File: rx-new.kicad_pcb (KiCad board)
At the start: 2 copper layers, 76.2 x 57.1 mm, 96 parts, among them J1 RF_IN, J2 PWR_IN, J3 IQ_OUT, J4 4LO_IN, Q1 BC848, Q2 BC858, Q3 BC848, Q4 BC858, U1 TPS79101DBVREP, U2 SN74CBT3253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

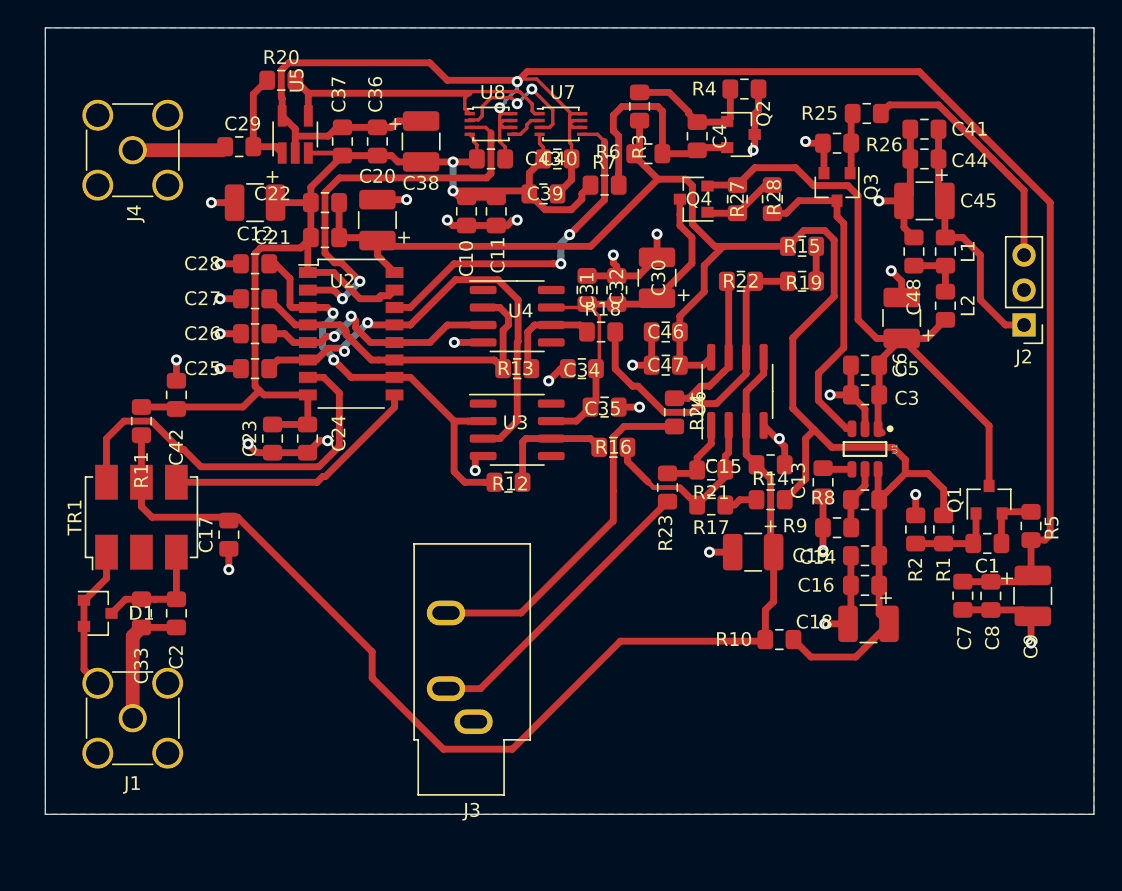
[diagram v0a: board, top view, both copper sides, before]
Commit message: Added mounting holes and small layout changes
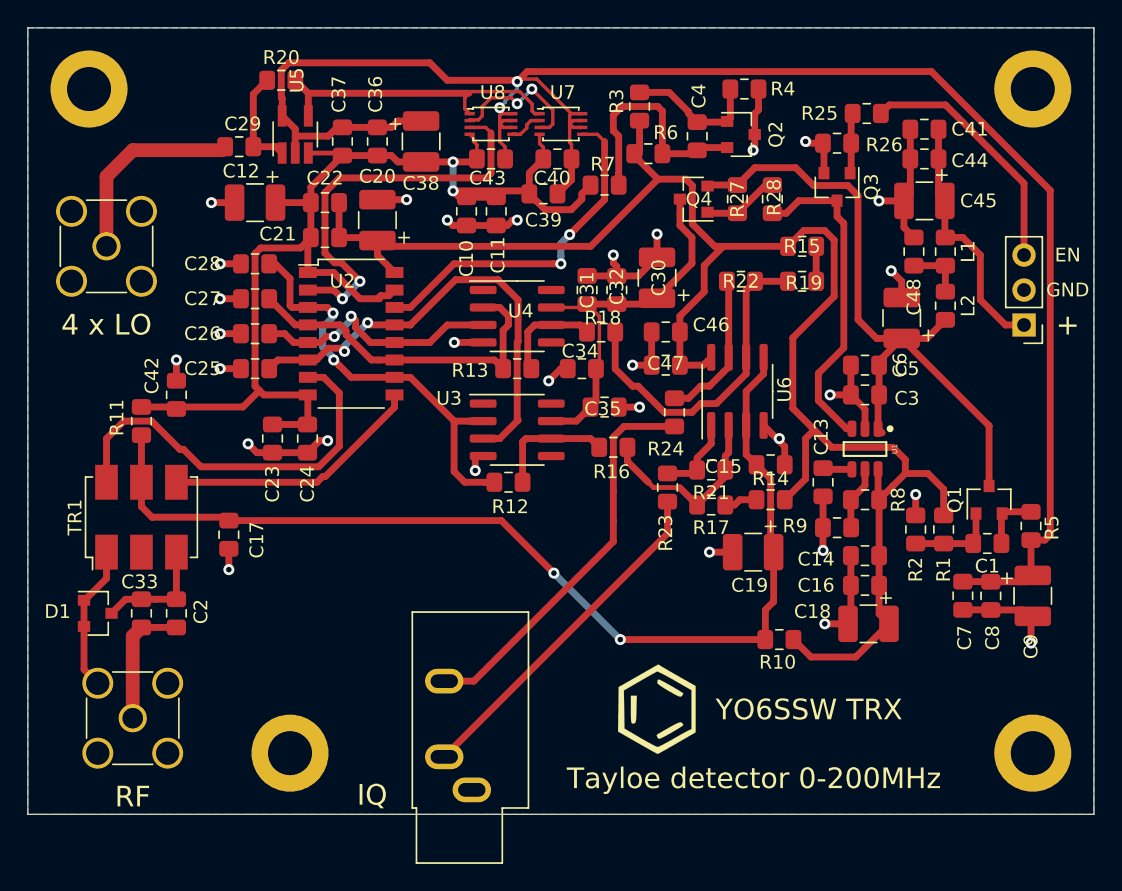
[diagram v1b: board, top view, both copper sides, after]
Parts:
- added G***: LOGO, benzen_logos:benzene_only_logo, F.Cu at (108.0, 94.0)
- added H1: MountingHole_Pad, MountingHole:MountingHole_3.2mm_M3_DIN965_Pad, F.Cu at (135.3, 48.9)
- added H2: MountingHole_Pad, MountingHole:MountingHole_3.2mm_M3_DIN965_Pad, F.Cu at (66.7, 48.9)
- added H3: MountingHole_Pad, MountingHole:MountingHole_3.2mm_M3_DIN965_Pad, F.Cu at (135.3, 97.2)
- added H4: MountingHole_Pad, MountingHole:MountingHole_3.2mm_M3_DIN965_Pad, F.Cu at (81.3, 97.2)
- moved J4 7.24 mm to (67.9, 60.3)
- moved J3 4.95 mm to (94.5, 99.8)
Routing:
- net Net-(C29-Pad2): track 6.82 -> 14.6 mm
- net /Vbias: track 85.0 -> 77.3 mm, vias 0 -> 2
- net /AUDIO_I: track 22.0 -> 25.5 mm
- net /AUDIO_Q: track 25.8 -> 28.9 mm
- net /+Vd: track 134.0 -> 134.5 mm
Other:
- board size 76.2 x 57.1 mm -> 77.5 x 57.1 mm
- board text added: "+"
- board text added: "4 x LO"
- board text added: "EN"
- board text added: "GND"
- board text added: "IQ"
- board text added: "RF"
- board text added: "Tayloe detector 0-200MHz"
- board text added: "YO6SSW TRX"

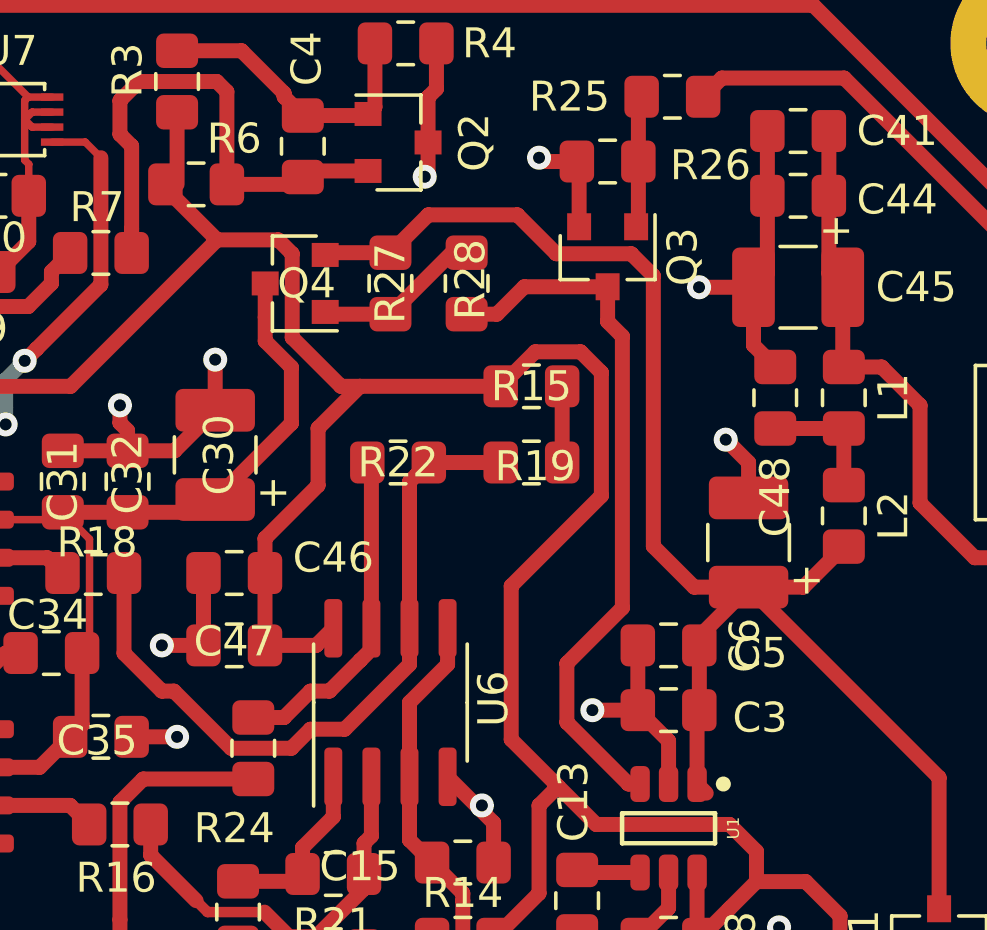
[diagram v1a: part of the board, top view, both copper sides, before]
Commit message: Updated voltages and updated opamp feedbacks + reworked En section
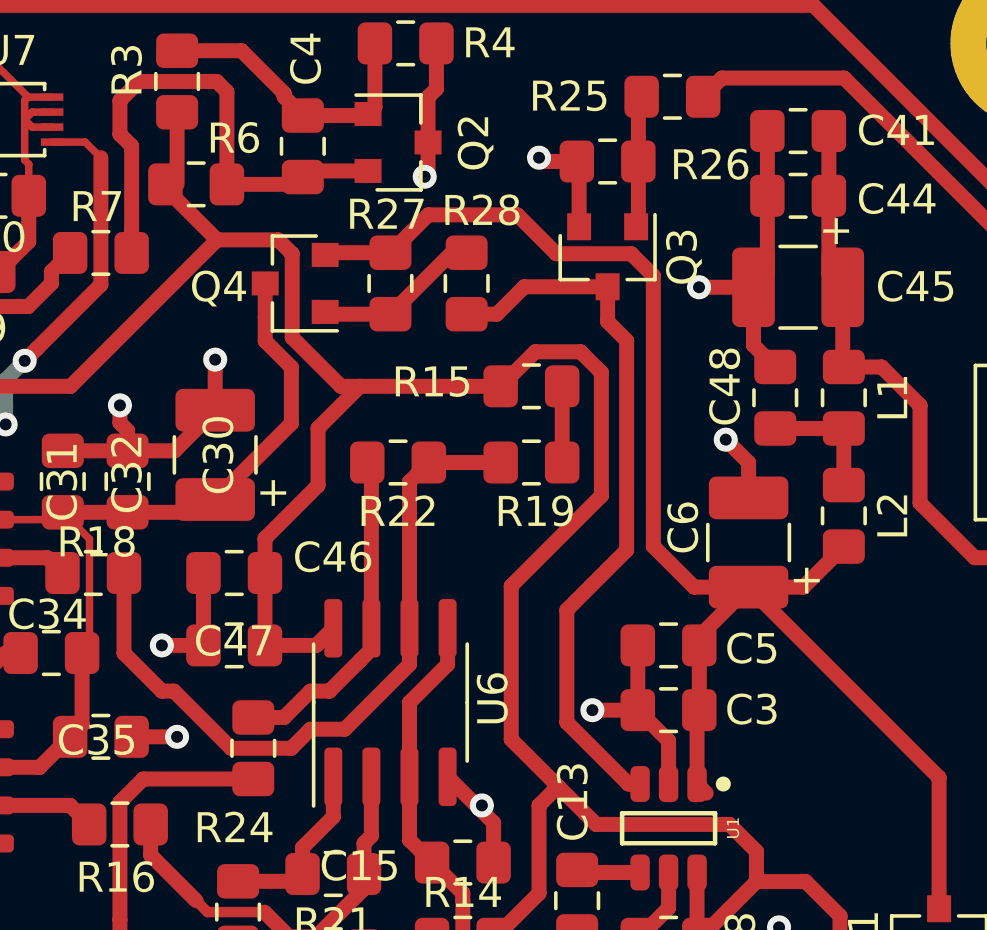
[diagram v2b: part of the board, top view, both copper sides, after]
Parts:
- R12, R13: value 1E -> 10k?
- R23, R24: value 1E -> 100E
- R3: value 100k -> 56k
- R4: value 100k -> 6k8
- R7: value 1E -> 22E
- R8: value 100k -> 120k
- R9: value 100k -> 27k
